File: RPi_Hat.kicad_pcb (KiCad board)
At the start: 2 copper layers, 65 x 56.5 mm, 38 parts, among them IC1 0.96_I2C_OLED, IC2 0.96_I2C_OLED, J1 RPi_GPIO, J2 TCBM, J3 Conn_01x05, J4 Mini-DIN-7, J5 Conn_01x07, Q1 MMBT3904, Q2 MMBT3904, Q3 MMBT3904, Q4 MMBT3904, SW1 Select, SW2 Up, SW3 Down, SW4 Exit, SW5 Add Disk, SW6 RotaryEncoder_Switch

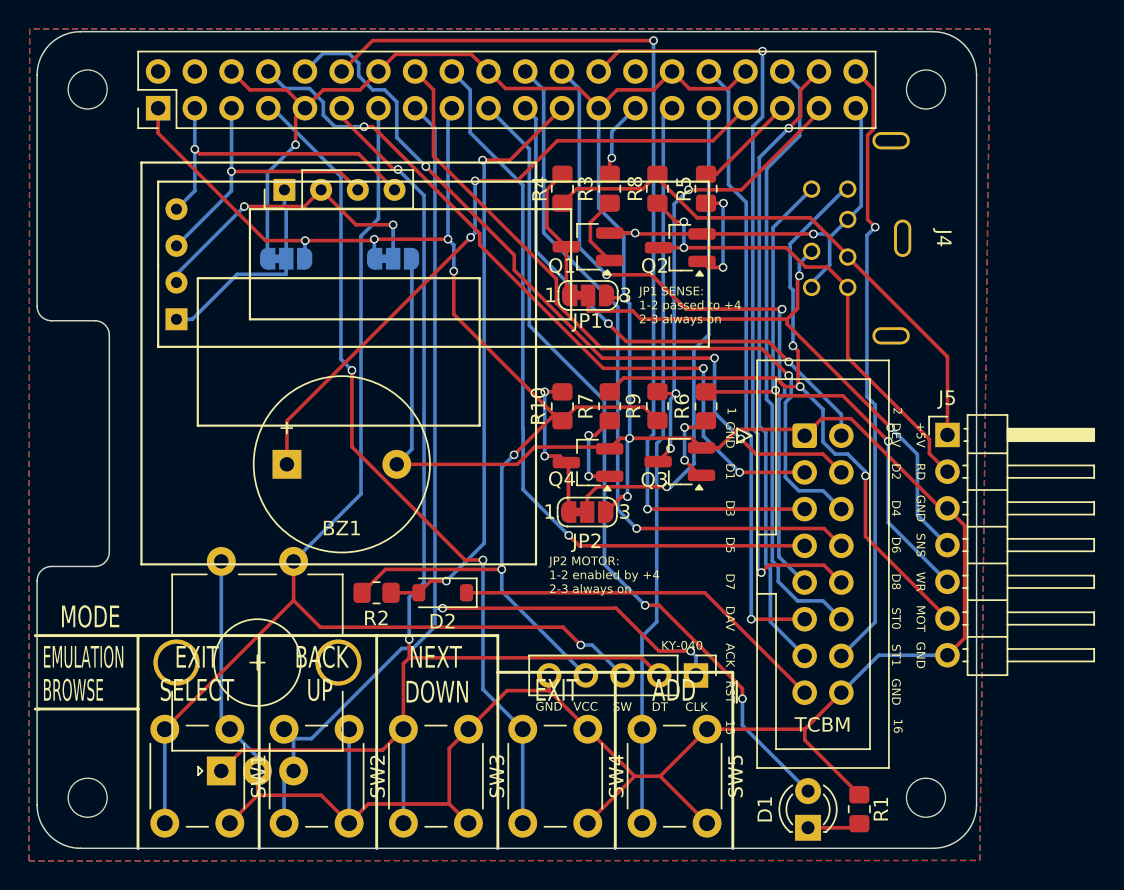
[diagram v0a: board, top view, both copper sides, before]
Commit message: TCBM pullups are required
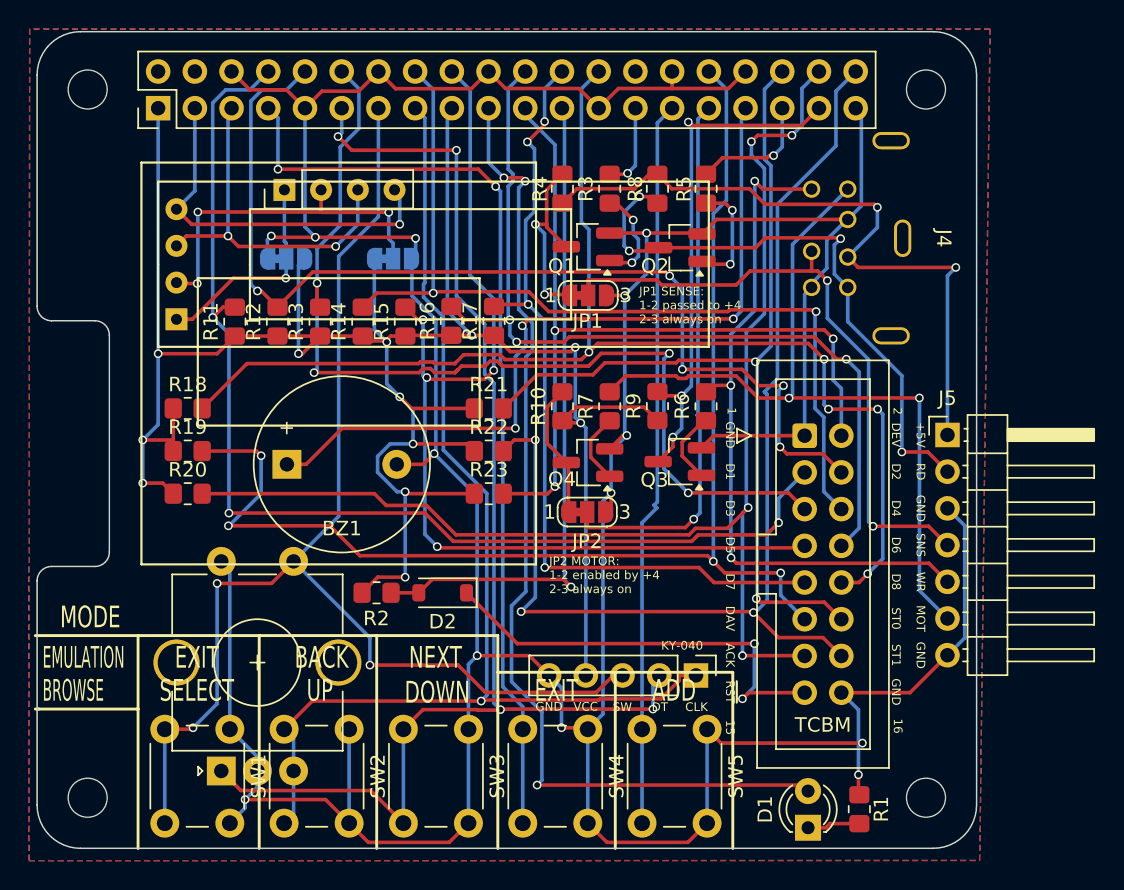
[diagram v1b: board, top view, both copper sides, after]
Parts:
- added R11: 10k, Resistor_SMD:R_0805_2012Metric_Pad1.20x1.40mm_HandSolder, F.Cu at (37.2, 48.6)
- added R12: 10k, Resistor_SMD:R_0805_2012Metric_Pad1.20x1.40mm_HandSolder, F.Cu at (40.1, 48.6)
- added R13: 10k, Resistor_SMD:R_0805_2012Metric_Pad1.20x1.40mm_HandSolder, F.Cu at (43.1, 48.6)
- added R14: 10k, Resistor_SMD:R_0805_2012Metric_Pad1.20x1.40mm_HandSolder, F.Cu at (46.0, 48.6)
- added R15: 10k, Resistor_SMD:R_0805_2012Metric_Pad1.20x1.40mm_HandSolder, F.Cu at (49.0, 48.6)
- added R16: 10k, Resistor_SMD:R_0805_2012Metric_Pad1.20x1.40mm_HandSolder, F.Cu at (52.2, 48.6)
- added R17: 10k, Resistor_SMD:R_0805_2012Metric_Pad1.20x1.40mm_HandSolder, F.Cu at (55.1, 48.6)
- added R18: 10k, Resistor_SMD:R_0805_2012Metric_Pad1.20x1.40mm_HandSolder, F.Cu at (33.9, 54.6)
- added R19: 10k, Resistor_SMD:R_0805_2012Metric_Pad1.20x1.40mm_HandSolder, F.Cu at (33.9, 57.6)
- added R20: 10k, Resistor_SMD:R_0805_2012Metric_Pad1.20x1.40mm_HandSolder, F.Cu at (33.9, 60.5)
- added R21: 10k, Resistor_SMD:R_0805_2012Metric_Pad1.20x1.40mm_HandSolder, F.Cu at (54.7, 54.6)
- added R22: 10k, Resistor_SMD:R_0805_2012Metric_Pad1.20x1.40mm_HandSolder, F.Cu at (54.7, 57.6)
- added R23: 10k, Resistor_SMD:R_0805_2012Metric_Pad1.20x1.40mm_HandSolder, F.Cu at (54.7, 60.5)
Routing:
- net +3V3: track 92.2 -> 165.8 mm, vias 6 -> 12
- net /ACK: track 43.4 -> 88.9 mm, vias 1 -> 4
- net /DAV: track 42.8 -> 88.3 mm, vias 1 -> 4
- net /STATUS1: track 42.8 -> 79.1 mm, vias 1 -> 3
- net /DIO8: track 54.8 -> 86.9 mm, vias 2 -> 5
- net /DIO1: track 52.3 -> 79.3 mm
- net GND: track 288.3 -> 314.2 mm, vias 6 -> 13
- net /STATUS0: track 42.5 -> 63.0 mm, vias 0 -> 2
- net /DEV: track 37.5 -> 57.3 mm, vias 2 -> 3
- net /DIO5: track 52.1 -> 70.1 mm, vias 1 -> 4
- net /DIO2: track 54.4 -> 71.7 mm, vias 3 -> 5
- net /RPI_LED: track 57.0 -> 69.7 mm, vias 2 -> 3
- net /DIO4: track 50.3 -> 62.8 mm, vias 1 -> 2
- net /DIO6: track 49.5 -> 61.5 mm, vias 1 -> 3
- net /VCC_5V: track 38.3 -> 47.5 mm, vias 0 -> 2
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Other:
- board text added: "Maciej Witkowiak <ytm@elysium.pl>, III 2026"
- board text removed: "Maciej Witkowiak <ytm@elysium.pl>, II 2026"
